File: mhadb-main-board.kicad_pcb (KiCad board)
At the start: 4 copper layers, 50 x 50 mm, 109 parts, among them J1 Conn_01x04, J10 Conn_01x04_Pin, J2 Conn_01x04, J3 USB_C_Receptacle_USB2.0_14P, J4 Conn_01x02, J5 Conn_01x03, J6 Conn_01x03, J7 Conn_01x04, J8 Conn_01x04, J9 Conn_01x02_Pin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

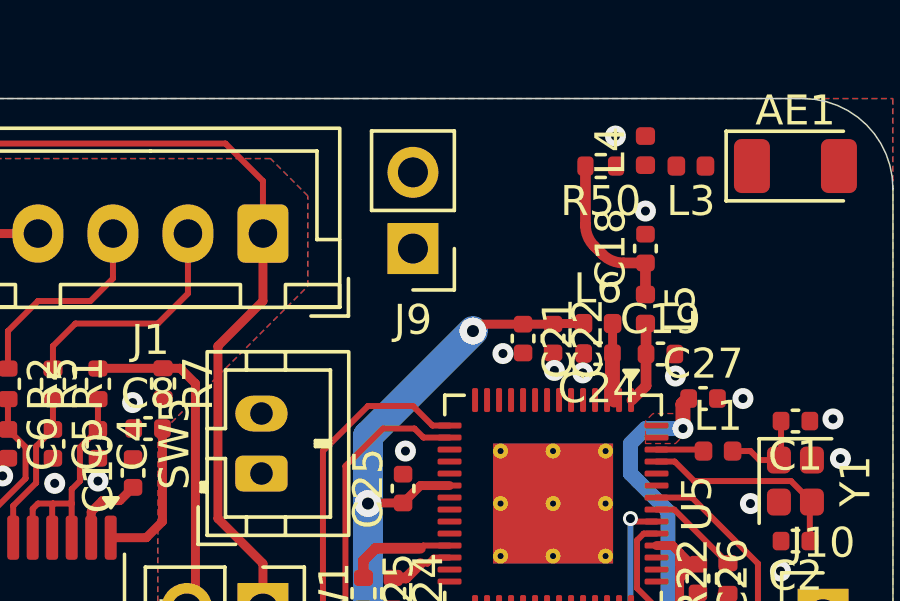
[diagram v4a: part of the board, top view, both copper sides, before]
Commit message: pcb: add spare GPIOs routing
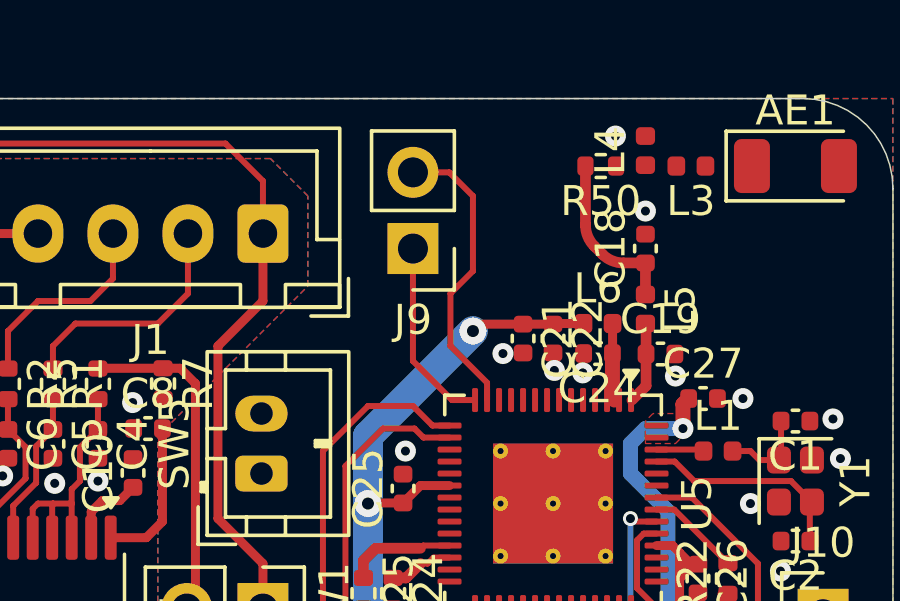
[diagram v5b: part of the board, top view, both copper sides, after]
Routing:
- net Net-(J9-Pin_2): track 0.00 -> 9.94 mm
- net Net-(J9-Pin_1): track 0.00 -> 6.36 mm
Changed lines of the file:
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@@
+	)
+	(segment
+		(start 139.25 56.5)
+		(end 140 55.75)
+		(width 0.2)
+		(layer "F.Cu")
+		(net 38)
+	)
+	(segment
+		(start 140.47 59.47)
+		(end 139.25 58.25)
+		(width 0.2)
+		(layer "F.Cu")
+		(net 38)
+	)
+	(segment
+		(start 139.25 58.25)
+		(end 139.25 56.5)
+		(width 0.2)
+		(layer "F.Cu")
+		(net 38)
+	)
+	(segment
+		(start 140 53.25)
+		(end 139.21 52.46)
+		(width 0.2)
+		(layer "F.Cu")
+		(net 38)
+	)
+	(segment
+		(start 140.47 60.05)
+		(end 140.47 59.47)
+		(width 0.2)
+		(layer "F.Cu")
+		(net 38)
+	)
+	(segment
+		(start 140 55.75)
+		(end 140 53.25)
+		(width 0.2)
+		(layer "F.Cu")
+		(net 38)
+	)
+	(segment
+		(start 139.21 52.46)
+		(end 138 52.46)
+		(width 0.2)
+		(layer "F.Cu")
+		(net 38)
+	)
+	(segment
+		(start 138 58.75)
+		(end 139.3 60.05)
+		(width 0.2)
+		(layer "F.Cu")
+		(net 39)
+	)
+	(segment
+		(start 139.3 60.05)
+		(end 140.07 60.05)
+		(width 0.2)
+		(layer "F.Cu")
+		(net 39)
+	)
+	(segment
+		(start 138 55)
+		(end 138 58.75)
+		(width 0.2)
+		(layer "F.Cu")
+		(net 39)
 	)
 	(segment

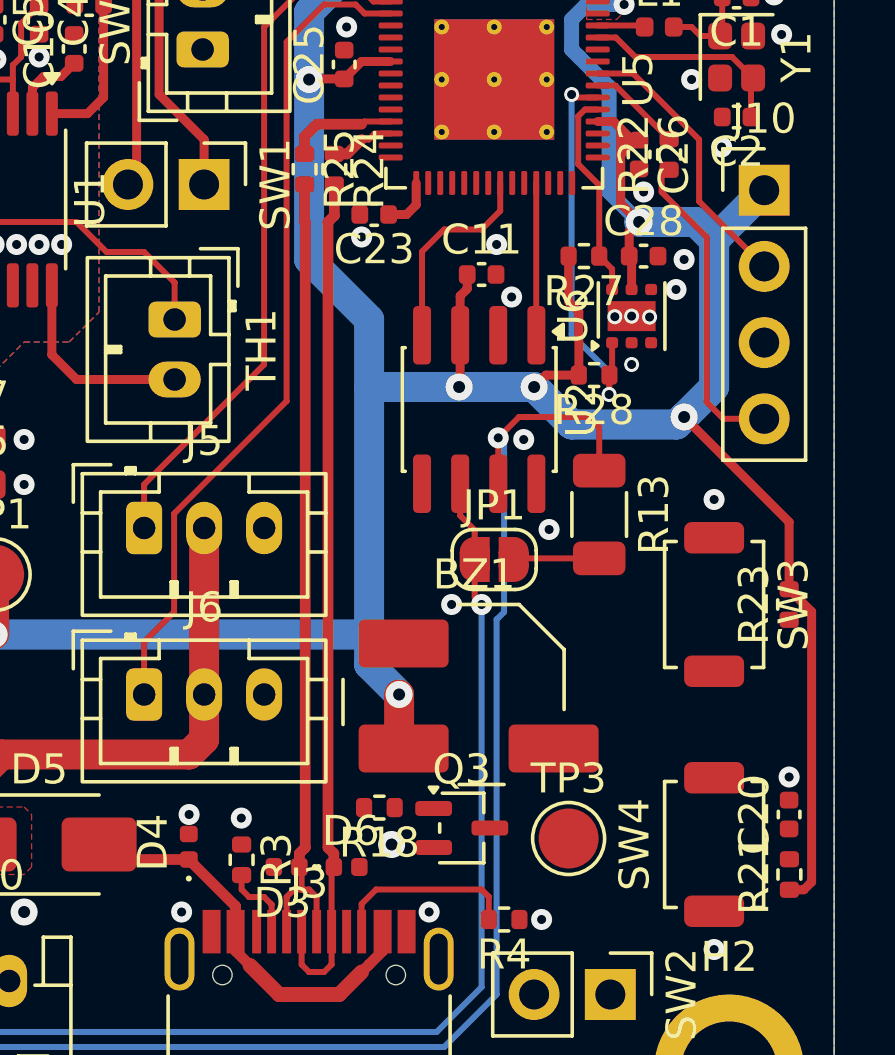
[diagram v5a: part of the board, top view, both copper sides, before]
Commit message: pcb: add buzzer routing
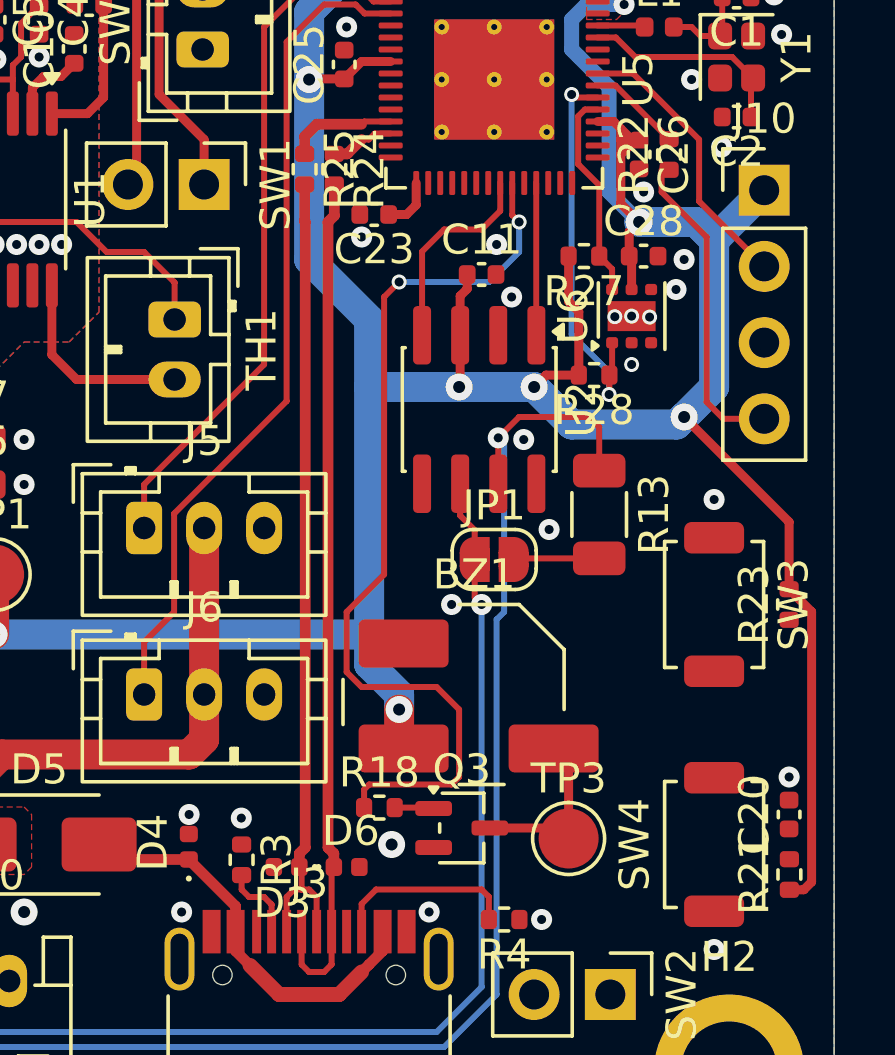
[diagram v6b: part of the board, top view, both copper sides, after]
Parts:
- turned R18 to 0 degrees
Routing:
- net /BUZZER: track 0.00 -> 31.0 mm, vias 0 -> 2
- net Net-(BZ1--): track 0.00 -> 5.98 mm
- net Net-(Q3-G): track 0.00 -> 1.31 mm
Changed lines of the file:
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@@
 	(footprint "Resistor_SMD:R_0402_1005Metric"
 		(layer "F.Cu")
-		(at 138.8425 87.77 180)
+		(at 138.8425 87.77)
 		(descr "Resistor SMD 0402 (1005 Metric), square (rectangular) end terminal, IPC-7351 nominal, (Body size source: IPC-SM-782 page 72, https://www.pcb-3d.com/wordpress/wp-content/uploads/ipc-sm-782a_amendment_1_and_2.pdf), generated with kicad-footprint-generator")
 		(tags "resistor")
@@
 		)
 		(property "Basic" "Y"
-			(at 0 0 180)
+			(at 0 0 0)
 			(unlocked yes)
 			(layer "F.Fab")
@@
 		)
 		(property "JLCPCB Part #" "C25123"
-			(at 0 0 180)
+			(at 0 0 0)
 			(unlocked yes)
 			(layer "F.Fab")
@@
 		)
 		(property "Manufacturer" "Uniroyal Elec"
-			(at 0 0 180)
+			(at 0 0 0)
 			(unlocked yes)
 			(layer "F.Fab")
@@
 		)
 		(property "Manufacturer Part Number" "0402WGF5100TCE"
-			(at 0 0 180)
+			(at 0 0 0)
 			(unlocked yes)
 			(layer "F.Fab")
@@
 		(attr smd)
 		(fp_line
-			(start -0.153641 0.38)
-			(end 0.153641 0.38)
+			(start -0.153641 -0.38)
+			(end 0.153641 -0.38)
 			(stroke
 				(width 0.12)
@@
 		)
 		(fp_line
-			(start -0.153641 -0.38)
-			(end 0.153641 -0.38)
+			(start -0.153641 0.38)
+			(end 0.153641 0.38)
 			(stroke
 				(width 0.12)
@@
 		)
 		(pad "1" smd roundrect
-			(at -0.51 0 180)
+			(at -0.51 0)
 			(size 0.54 0.64)
 			(layers "F.Cu" "F.Mask" "F.Paste")
@@
 		)
 		(pad "2" smd roundrect
-			(at 0.51 0 180)
+			(at 0.51 0)
 			(size 0.54 0.64)
 			(layers "F.Cu" "F.Mask" "F.Paste")
@@
 	)
 	(segment
+		(start 145.15 86.3)
+		(end 144.65 85.8)
+		(width 0.2)
+		(layer "F.Cu")
+		(net 2)
+	)
+	(segment
+		(start 145.15 88.8)
+		(end 145.15 86.3)
+		(width 0.3)
+		(layer "F.Cu")
+		(net 2)
+	)
+	(segment
+		(start 144.8 88.45)
+		(end 145.15 88.8)
+		(width 0.2)
+		(layer "F.Cu")
+		(net 2)
+	)
+	(segment
+		(start 142.525 88.45)
+		(end 144.8 88.45)
+		(width 0.3)
+		(layer "F.Cu")
+		(net 2)
+	)
+	(segment
 		(start 147.5 65.52)
 		(end 146.909 65.52)
@@
 	)
 	(segment
-		(start 139.5 84)
-		(end 139.5 85.65)
-		(width 1)
-		(layer "F.Cu")
-		(net 3)
-	)
-	(segment
 		(start 141.535 73.715)
 		(end 141.5 73.75)
@@
 	)
 	(segment
+		(start 139.5 84.5)
+		(end 139.5 85.65)
+		(width 1)
+		(layer "F.Cu")
+		(net 3)
+	)
+	(segment
 		(start 147.5 68.25)
 		(end 146.889 67.639)
@@
 	)
 	(segment
-		(start 139.5 85.65)
-		(end 139.65 85.8)
-		(width 1)
-		(layer "F.Cu")
-		(net 3)
-	)
-	(segment
 		(start 139.22 62.9)
 		(end 138.25 62.9)
@@
 	)
 	(segment
+		(start 139.5 85.65)
+		(end 139.65 85.8)
+		(width 1)
+		(layer "F.Cu")
+		(net 3)
+	)
+	(segment
 		(start 147.369 65.52)
 		(end 146.889 66)
@@
 	)
 	(via
-		(at 139.5 84)
+		(at 139.5 84.5)
 		(size 0.9)
 		(drill 0.4)
@@
 	)
 	(segment
+		(start 139.5 84.5)
+		(end 139.5 84)
+		(width 1)
+		(layer "B.Cu")
+		(net 3)
+	)
+	(segment
 		(start 138.5 73.75)
 		(end 138.5 71.5)
@@
 	)
 	(segment
-		(start 138.5 82)
-		(end 138.5 83)
+		(start 145.25 75)
+		(end 148.75 75)
 		(width 1)
 		(layer "B.Cu")
@@
 	)
 	(segment
-		(start 145.25 75)
-		(end 148.75 75)
+		(start 138.5 83)
+		(end 138.5 82)
 		(width 1)
 		(layer "B.Cu")
@@
 	)
 	(segment
-		(start 138.5 71.5)
-		(end 136.5 69.5)
+		(start 139.5 84)
+		(end 138.5 83)
 		(width 1)
 		(layer "B.Cu")
@@
 	)
 	(segment
-		(start 138.5 83)
-		(end 139.5 84)
+		(start 138.5 71.5)
+		(end 136.5 69.5)
 		(width 1)
 		(layer "B.Cu")
@@
 	)
 	(segment
+		(start 140.62 87.77)
+		(end 140.65 87.8)
+		(width 0.2)
+		(layer "F.Cu")
+		(net 47)
+	)
+	(segment
+		(start 139.3525 87.77)
+		(end 140.62 87.77)
+		(width 0.2)
+		(layer "F.Cu")
+		(net 47)
+	)
+	(segment
 		(start 130.75 66.71)
 		(end 130.46 67)
@@
 	)
 	(segment
+		(start 138.3325 87.77)
+		(end 138.3325 87.1675)
+		(width 0.2)
+		(layer "F.Cu")
+		(net 54)
+	)
+	(segment
+		(start 139 70.75)
+		(end 139.5 70.25)
+		(width 0.2)
+		(layer "F.Cu")
+		(net 54)
+	)
+	(segment
+		(start 137.75 81.25)
+		(end 139 80)
+		(width 0.2)
+		(layer "F.Cu")
+		(net 54)
+	)
+	(segment
+		(start 141.5 84.5)
+		(end 140.75 83.75)
+		(width 0.2)
+		(layer "F.Cu")
+		(net 54)
+	)
+	(segment
+		(start 138.3325 87.1675)
+		(end 138.5 87)
+		(width 0.2)
+		(layer "F.Cu")
+		(net 54)
+	)
+	(segment
+		(start 138.5 87)
+		(end 141.25 87)
+		(width 0.2)
+		(layer "F.Cu")
+		(net 54)
+	)
+	(segment
+		(start 139 80)
+		(end 139 70.75)
+		(width 0.2)
+		(layer "F.Cu")
+		(net 54)
+	)
+	(segment
+		(start 143.27 68.02)
+		(end 143.5 68.25)
+		(width 0.2)
+		(layer "F.Cu")
+		(net 54)
+	)
+	(segment
+		(start 140.75 83.75)
+		(end 138.25 83.75)
+		(width 0.2)
+		(layer "F.Cu")
+		(net 54)
+	)
+	(segment
+		(start 137.75 83.25)
+		(end 137.75 81.25)
+		(width 0.2)
+		(layer "F.Cu")
+		(net 54)
+	)
+	(segment
+		(start 143.27 66.95)
+		(end 143.27 68.02)
+		(width 0.2)
+		(layer "F.Cu")
+		(net 54)
+	)
+	(segment
+		(start 141.5 86.75)
+		(end 141.5 84.5)
+		(width 0.2)
+		(layer "F.Cu")
+		(net 54)
+	)
+	(segment
+		(start 141.25 87)
+		(end 141.5 86.75)
+		(width 0.2)
+		(layer "F.Cu")
+		(net 54)
+	)
+	(segment
+		(start 138.25 83.75)
+		(end 137.75 83.25)
+		(width 0.2)
+		(layer "F.Cu")
+		(net 54)
+	)
+	(via
+		(at 139.5 70.25)
+		(size 0.5)
+		(drill 0.3)
+		(layers "F.Cu" "B.Cu")
+		(net 54)
+	)
+	(via
+		(at 143.5 68.25)
+		(size 0.5)
+		(drill 0.3)
+		(layers "F.Cu" "B.Cu")
+		(net 54)
+	)
+	(segment
+		(start 143.5 69.25)
+		(end 142.75 70)
+		(width 0.2)
+		(layer "B.Cu")
+		(net 54)
+	)
+	(segment
+		(start 142.5 70.25)
+		(end 139.5 70.25)
+		(width 0.2)
+		(layer "B.Cu")
+		(net 54)
+	)
+	(segment
+		(start 143.5 68.25)
+		(end 143.5 69.25)
+		(width 0.2)
+		(layer "B.Cu")
+		(net 54)
+	)
+	(segment
+		(start 142.75 70)
+		(end 142.5 70.25)
+		(width 0.2)
+		(layer "B.Cu")
+		(net 54)
+	)
+	(segment

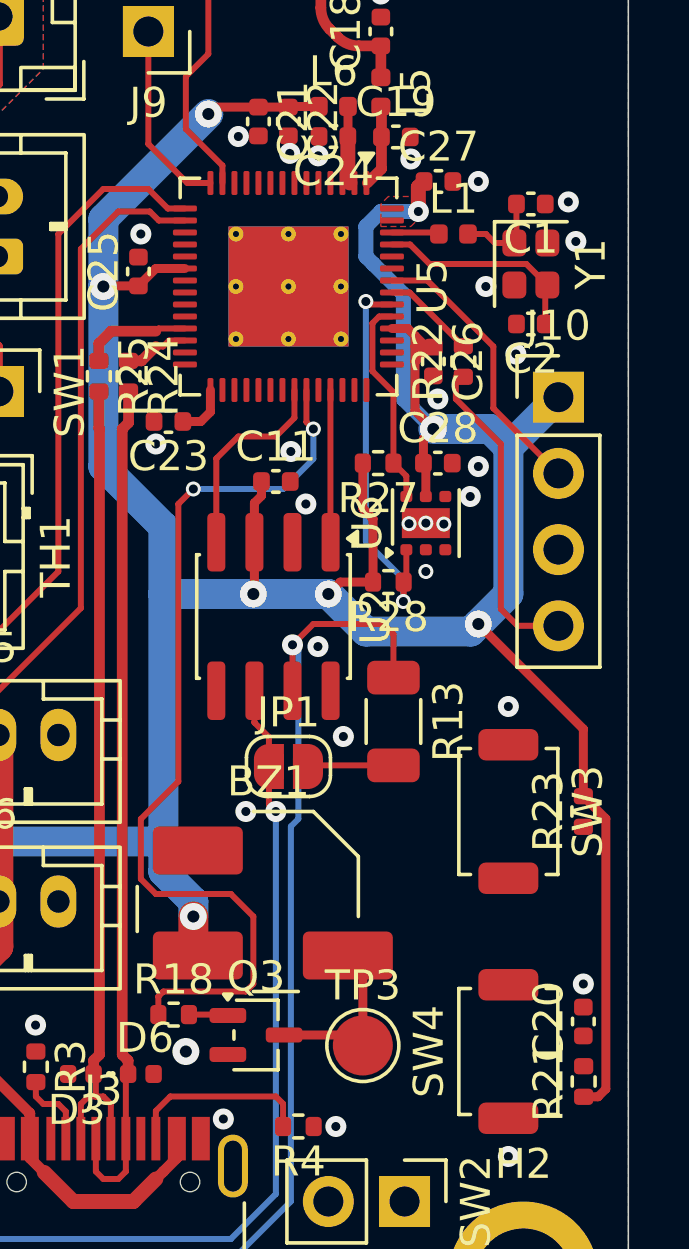
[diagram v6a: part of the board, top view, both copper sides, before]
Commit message: pcb: add BOOT and CHIP_PU routing
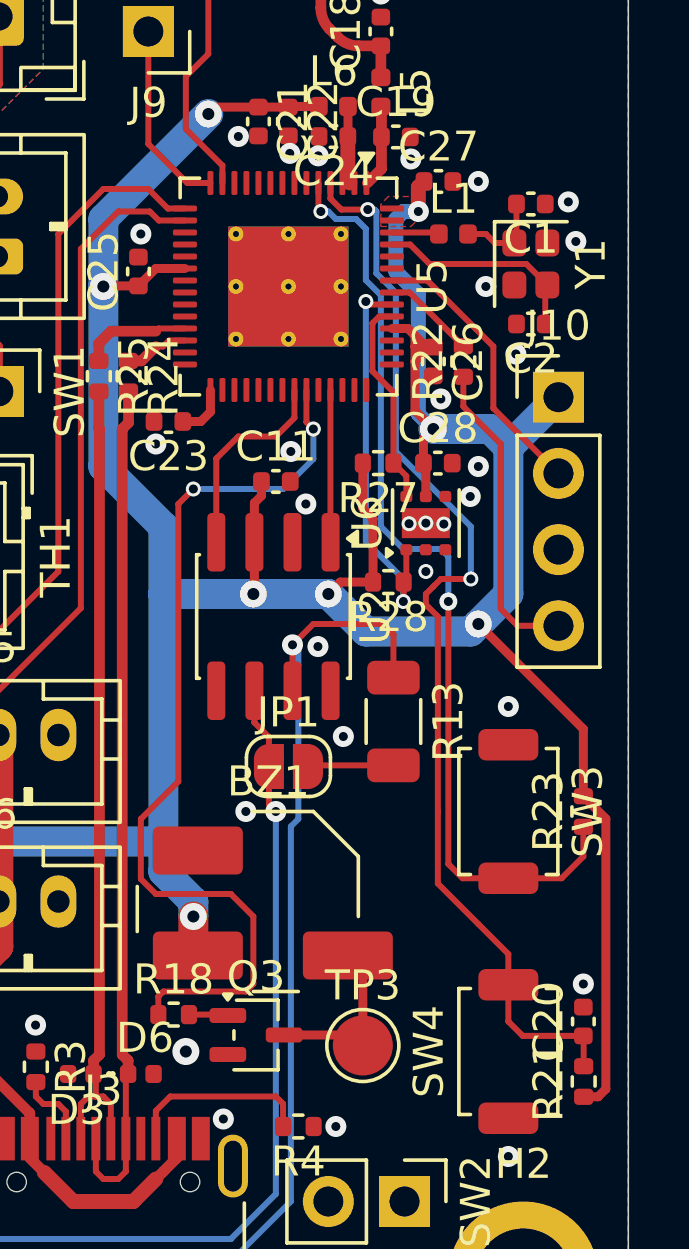
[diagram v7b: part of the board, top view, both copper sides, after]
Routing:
- net /CHIP_PU: track 0.00 -> 36.6 mm, vias 0 -> 2
- net /BOOT: track 0.00 -> 31.8 mm, vias 0 -> 2
- net +3V3: track 125.6 -> 124.3 mm

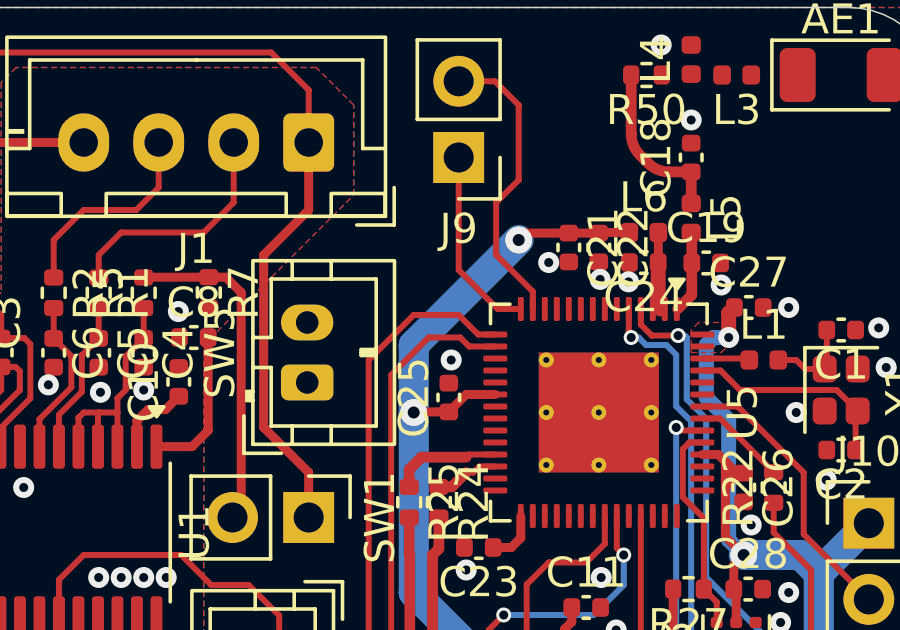
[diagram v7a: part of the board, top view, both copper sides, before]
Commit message: pcb: add EMS button routing
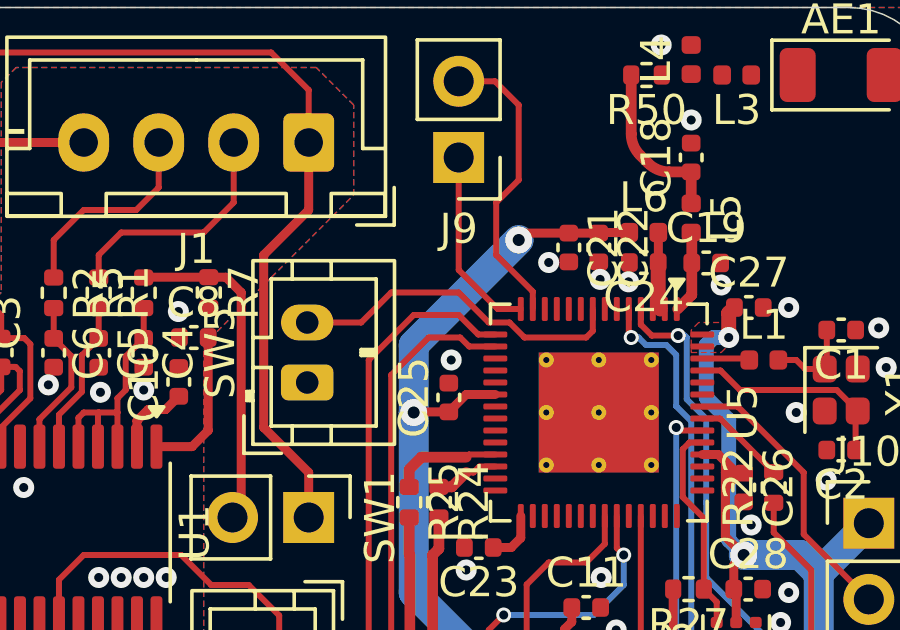
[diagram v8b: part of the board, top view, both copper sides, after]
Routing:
- net /EMS: track 0.00 -> 11.4 mm
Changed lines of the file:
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@@
+	)
+	(segment
+		(start 132.95 60.5)
+		(end 134.75 60.5)
+		(width 0.2)
+		(layer "F.Cu")
+		(net 61)
+	)
+	(segment
+		(start 134.75 60.5)
+		(end 135.75 59.5)
+		(width 0.2)
+		(layer "F.Cu")
+		(net 61)
+	)
+	(segment
+		(start 138 59.5)
+		(end 139 60.5)
+		(width 0.2)
+		(layer "F.Cu")
+		(net 61)
+	)
+	(segment
+		(start 139.692936 60.5)
+		(end 140.192936 61)
+		(width 0.2)
+		(layer "F.Cu")
+		(net 61)
+	)
+	(segment
+		(start 135.75 59.5)
+		(end 138 59.5)
+		(width 0.2)
+		(layer "F.Cu")
+		(net 61)
+	)
+	(segment
+		(start 142.47 60.78)
+		(end 142.47 60.05)
+		(width 0.2)
+		(layer "F.Cu")
+		(net 61)
+	)
+	(segment
+		(start 139 60.5)
+		(end 139.692936 60.5)
+		(width 0.2)
+		(layer "F.Cu")
+		(net 61)
+	)
+	(segment
+		(start 142.25 61)
+		(end 142.47 60.78)
+		(width 0.2)
+		(layer "F.Cu")
+		(net 61)
+	)
+	(segment
+		(start 140.192936 61)
+		(end 142.25 61)
+		(width 0.2)
+		(layer "F.Cu")
+		(net 61)
 	)
 	(segment
